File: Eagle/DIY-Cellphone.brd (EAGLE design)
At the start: 130.8 x 58.4 mm, 67 parts, among them IC1 MEGA1284, J1 ISP, U1 MCP73831, X1 BU-SMA-V, X3 CCM03-3002 R102

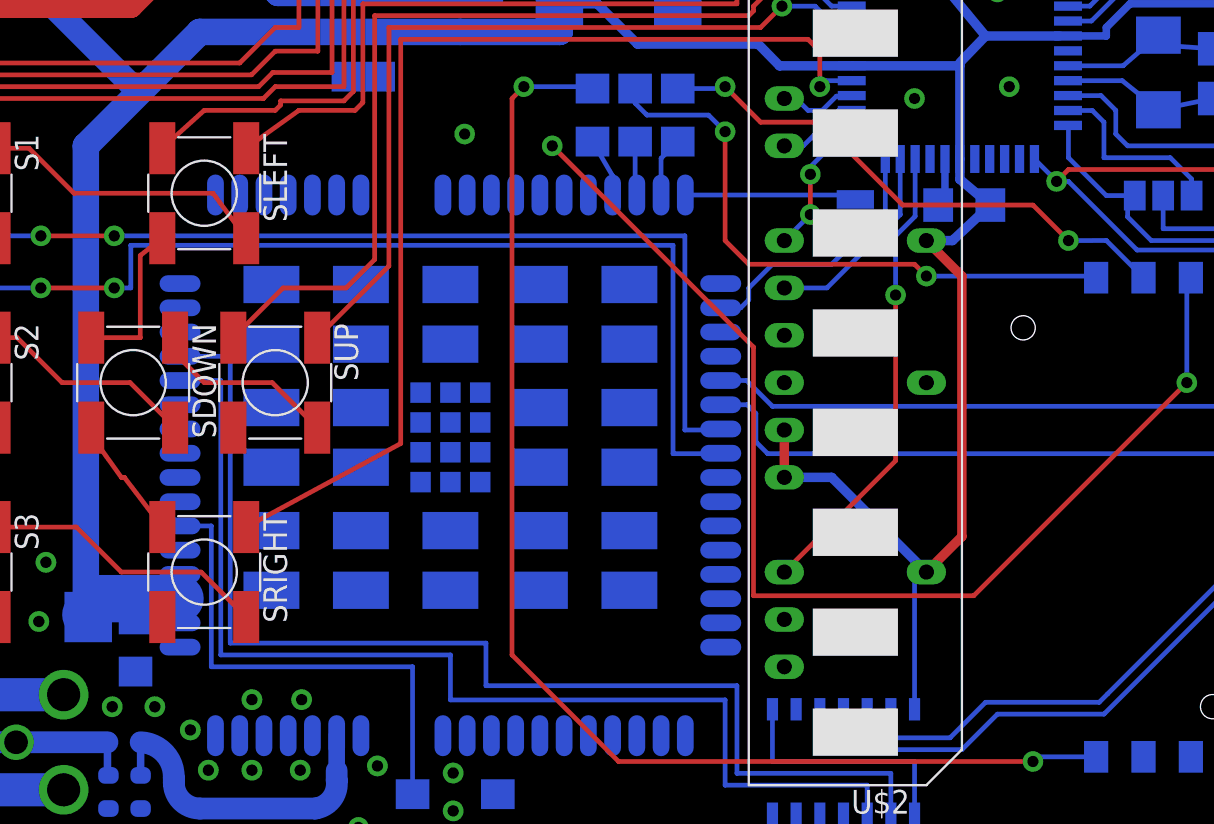
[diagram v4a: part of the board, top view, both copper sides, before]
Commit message: Add transistors and finish routing.
PWRKEY and RESET_N now have transistors between UC15 module and
ATmega1284.
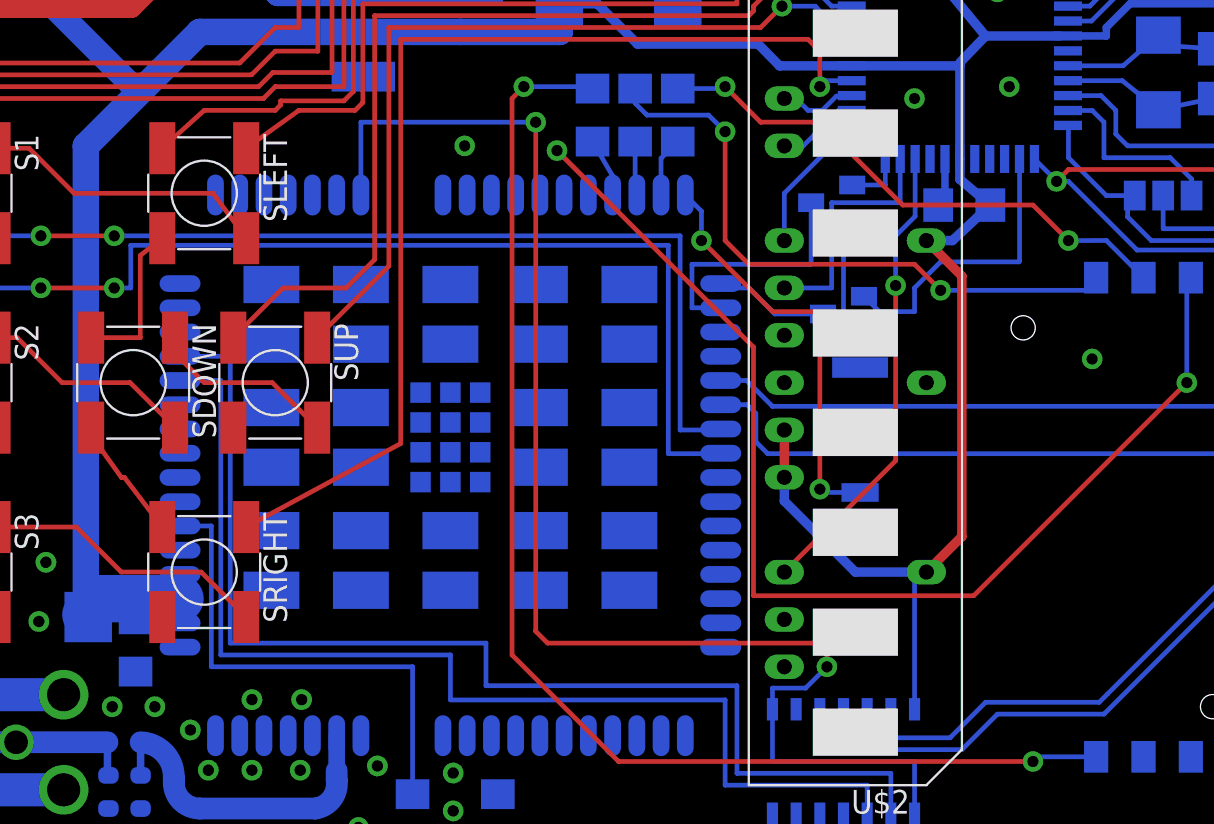
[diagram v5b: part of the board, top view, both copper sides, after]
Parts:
- added T2, T3: (no value), transistor:SOT23-BEC
- moved U$4 9.02 mm to (96.1, 26.7), turned to 90 degrees
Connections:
- net N$2 renamed VDD_EXT
- new net PWRKEY_PULLDOWN: IC1.22, T2.B
- new net RESET_N: T3.C, U$6.P$17
- new net RESET_N_PULLDOWN: IC1.13, T3.B
- net GND: now also T2.E, T3.E
- net PWRKEY: now also T2.C; no longer IC1.22
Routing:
- net VDD_EXT: track 13.2 -> 75.3 mm, vias 0 -> 2
- net RESET_N_PULLDOWN: track 0.00 -> 16.0 mm
- net VRTC: track 9.22 -> 22.5 mm, vias 0 -> 2
- net GND: track 117.6 -> 125.5 mm, vias 32 -> 33
- net RESET_N: track 0.00 -> 6.16 mm
- net PWRKEY_PULLDOWN: track 0.00 -> 3.17 mm
- net DISPLAY_CE: track 10.8 -> 13.1 mm
- net SIM_CLKR: track 32.8 -> 33.8 mm
- net VCC: track 251.9 -> 252.7 mm
- net SIM_VDD: track 65.8 -> 65.1 mm
- net PWRKEY: track 14.1 -> 13.6 mm
- net DISPLAY_CLOCK: vias 2 -> 0

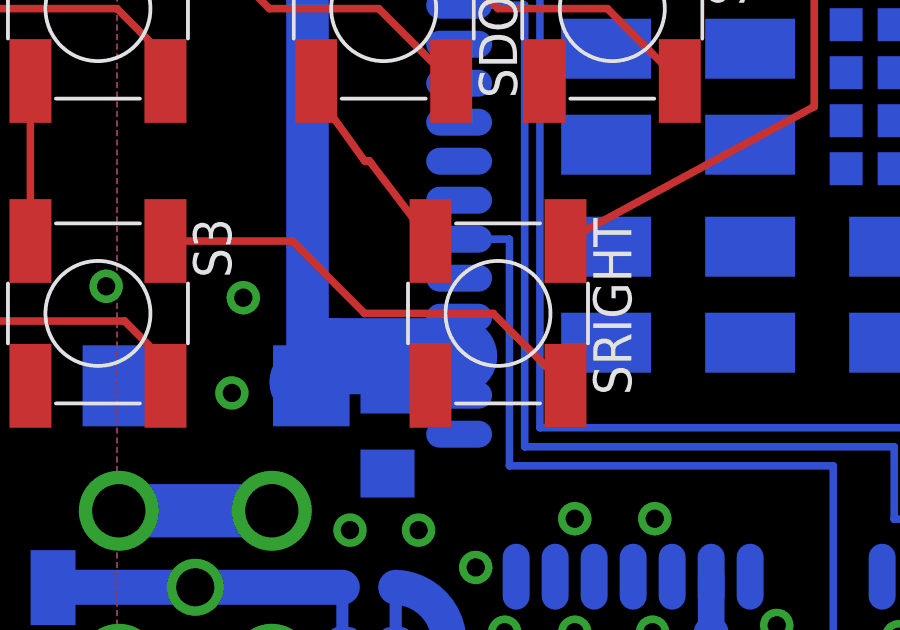
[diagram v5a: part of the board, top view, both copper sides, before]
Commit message: Connect fourth VCC pin and additional GND pins.
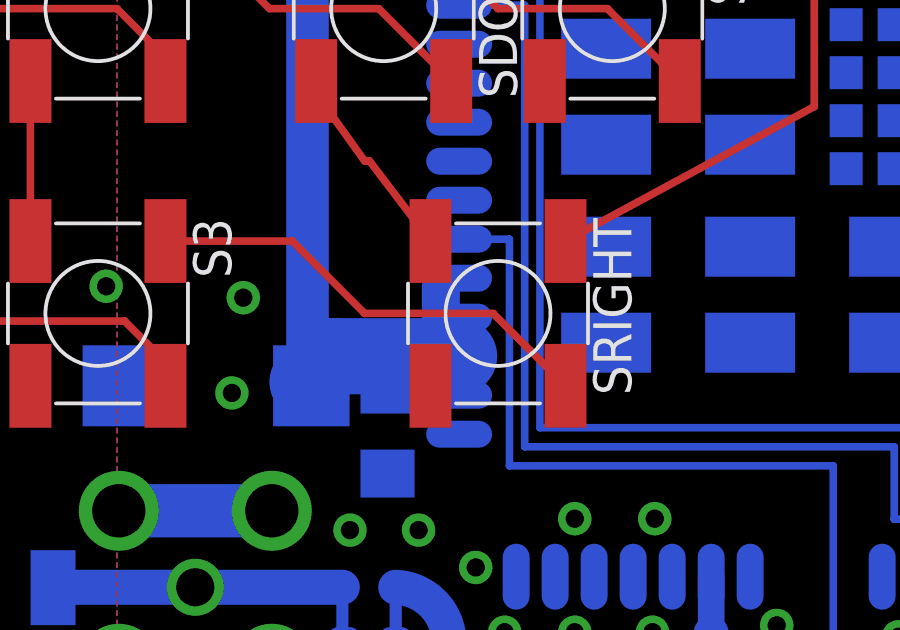
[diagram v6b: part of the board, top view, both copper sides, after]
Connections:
- net GND: now also U$6.P$100, U$6.P$101, U$6.P$102, U$6.P$103, U$6.P$104, U$6.P$105, U$6.P$106, U$6.P$107, U$6.P$108, U$6.P$65, U$6.P$67, U$6.P$68, U$6.P$81, U$6.P$82, U$6.P$83, U$6.P$84, U$6.P$85, U$6.P$86, U$6.P$87, U$6.P$88, U$6.P$89, U$6.P$90, U$6.P$91, U$6.P$92, U$6.P$93, U$6.P$94, U$6.P$95, U$6.P$96, U$6.P$97, U$6.P$98, U$6.P$99
- net VCC: now also U$6.P$53
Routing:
- net VCC: track 252.7 -> 255.7 mm
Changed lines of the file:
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@@
 <wire x1="107.292" y1="47.806" x2="109.347" y2="47.806" width="0.4064" layer="16"/>
 <contactref element="C16" pad="+"/>
-<wire x1="59.665" y1="18.924" x2="59.665" y2="17.624" width="0.4064" layer="16"/>
+<wire x1="59.665" y1="18.924" x2="59.665" y2="18.415" width="0.4064" layer="16"/>
+<wire x1="59.665" y1="18.415" x2="59.665" y2="17.624" width="0.4064" layer="16"/>
 <wire x1="59.665" y1="17.624" x2="59.665" y2="16.324" width="0.4064" layer="16"/>
 <via x="127" y="49.53" extent="1-16" drill="0.6"/>
@@
 <wire x1="92.075" y1="22.86" x2="95.885" y2="19.05" width="0.508" layer="16"/>
 <wire x1="95.885" y1="19.05" x2="99.695" y2="19.05" width="0.508" layer="16"/>
+<contactref element="U$6" pad="P$53"/>
+<wire x1="59.665" y1="20.224" x2="59.055" y2="20.224" width="0.4064" layer="16"/>
+<wire x1="59.055" y1="20.224" x2="59.055" y2="19.939" width="0.4064" layer="16"/>
+<wire x1="59.055" y1="19.939" x2="59.055" y2="18.415" width="1.27" layer="16"/>
+<wire x1="59.055" y1="18.415" x2="59.665" y2="18.415" width="1.27" layer="16"/>
 </signal>
 <signal name="ANT" class="4">
@@
 <wire x1="95.715" y1="38.1" x2="95.715" y2="37.912" width="0.254" layer="16"/>
 <via x="108.585" y="30.48" extent="1-16" drill="0.6"/>
+<contactref element="U$6" pad="P$67"/>
+<contactref element="U$6" pad="P$68"/>
+<contactref element="U$6" pad="P$65"/>
+<contactref element="U$6" pad="P$81"/>
+<contactref element="U$6" pad="P$94"/>
+<contactref element="U$6" pad="P$90"/>
+<contactref element="U$6" pad="P$85"/>
+<contactref element="U$6" pad="P$108"/>
+<contactref element="U$6" pad="P$103"/>
+<contactref element="U$6" pad="P$107"/>
+<contactref element="U$6" pad="P$98"/>
+<contactref element="U$6" pad="P$102"/>
+<contactref element="U$6" pad="P$97"/>
+<contactref element="U$6" pad="P$93"/>
+<contactref element="U$6" pad="P$89"/>
+<contactref element="U$6" pad="P$84"/>
+<contactref element="U$6" pad="P$106"/>
+<contactref element="U$6" pad="P$101"/>
+<contactref element="U$6" pad="P$88"/>
+<contactref element="U$6" pad="P$83"/>
+<contactref element="U$6" pad="P$105"/>
+<contactref element="U$6" pad="P$100"/>
+<contactref element="U$6" pad="P$96"/>
+<contactref element="U$6" pad="P$92"/>
+<contactref element="U$6" pad="P$87"/>
+<contactref element="U$6" pad="P$82"/>
+<contactref element="U$6" pad="P$104"/>
+<contactref element="U$6" pad="P$99"/>
+<contactref element="U$6" pad="P$95"/>
+<contactref element="U$6" pad="P$91"/>
+<contactref element="U$6" pad="P$86"/>
+<wire x1="74.165" y1="34.474" x2="73.765" y2="39.274" width="0" layer="19" extent="16-16"/>
 </signal>
 <signal name="DISP_DATA">
